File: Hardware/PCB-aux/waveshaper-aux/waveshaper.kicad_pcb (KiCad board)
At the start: 2 copper layers, 189 x 174 mm, 60 parts, among them J1 2x7 IDC header, J10 AudioJack2_SwitchT, J11 2_pin_Molex_header, J12 AudioJack2_SwitchT, J13 3_pin_Molex_header, J14 2x5 pin socket, J15 AudioJack2_SwitchT, J16 AudioJack2_SwitchT, J17 AudioJack2_SwitchT, J18 AudioJack2_SwitchT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

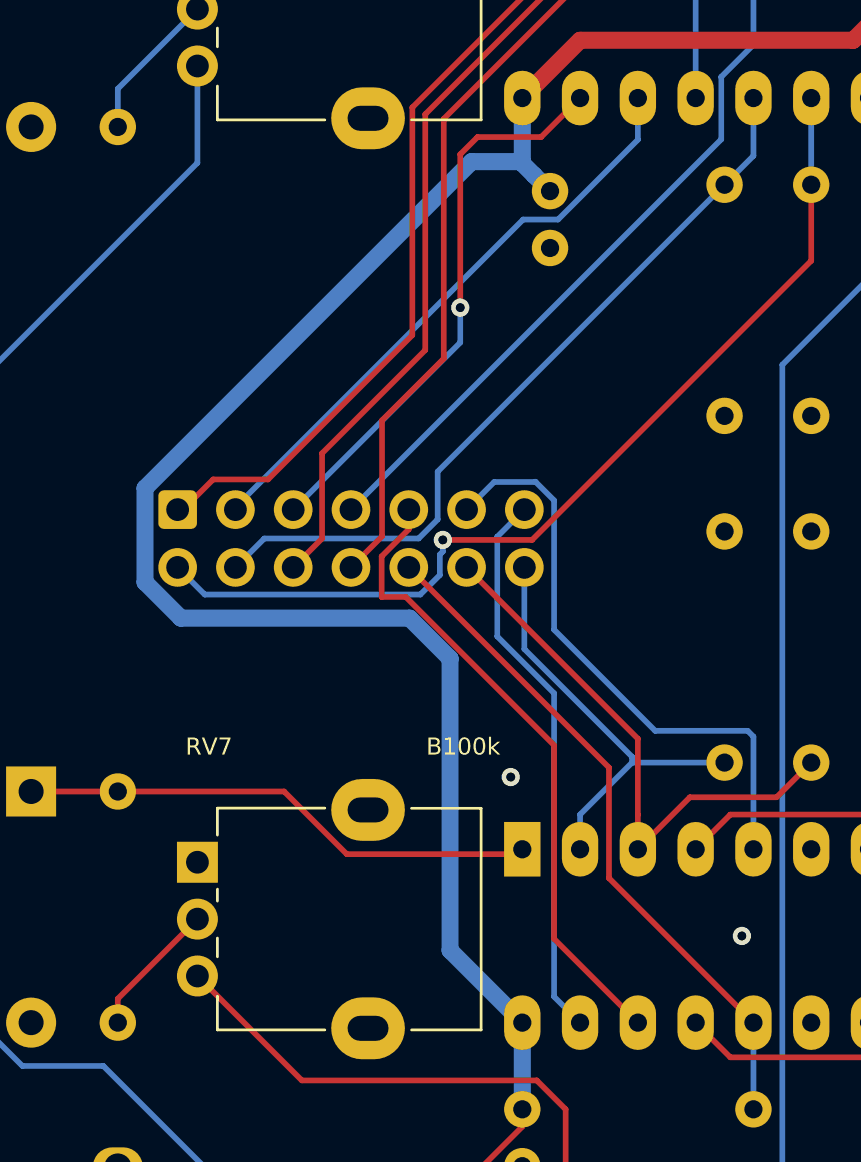
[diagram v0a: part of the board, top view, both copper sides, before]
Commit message: Pre fab tweaks, new Gerbers, clarify schematic for jacks connections
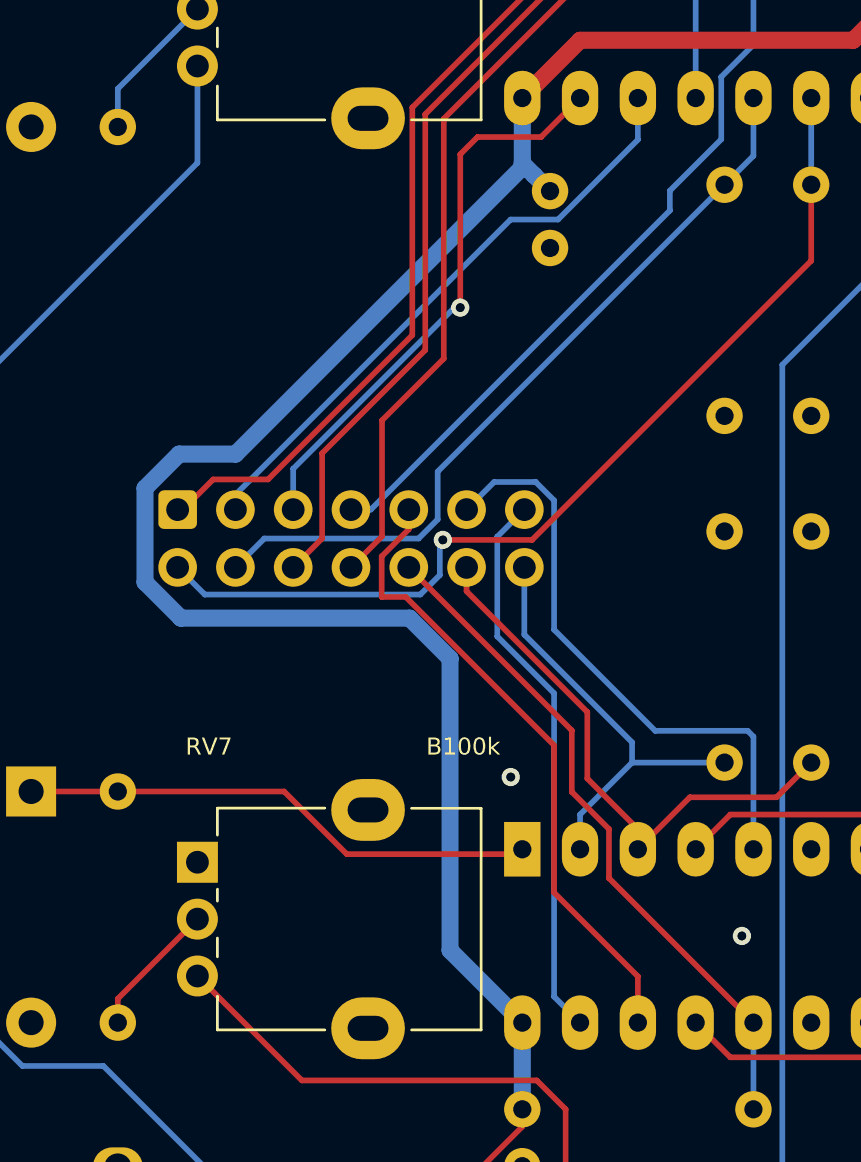
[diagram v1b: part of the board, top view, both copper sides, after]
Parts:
- J3, J4: value AudioJack2_SwitchT -> AudioJack2
- moved GRAF1 48.0 mm to (145.0, 54.4), turned to 180 degrees
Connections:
- net Net-(J10-PadTN) renamed J10V
- J3 pad TN: Net-(J3-PadTN) -> (no net)
- J4 pad TN: Net-(J4-PadTN) -> (no net)
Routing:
- net /RIPOUT_0: track 33.0 -> 33.5 mm
